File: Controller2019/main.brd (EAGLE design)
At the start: 85 x 65 mm, 95 parts, among them Q1 IPT007N06N, Q2 IPT007N06N, Q3 IPT007N06N, Q4 IPT007N06N, Q5 IPT007N06N, Q6 IPT007N06N, U1 TEENSY_3.0+4, U2 DRV8301

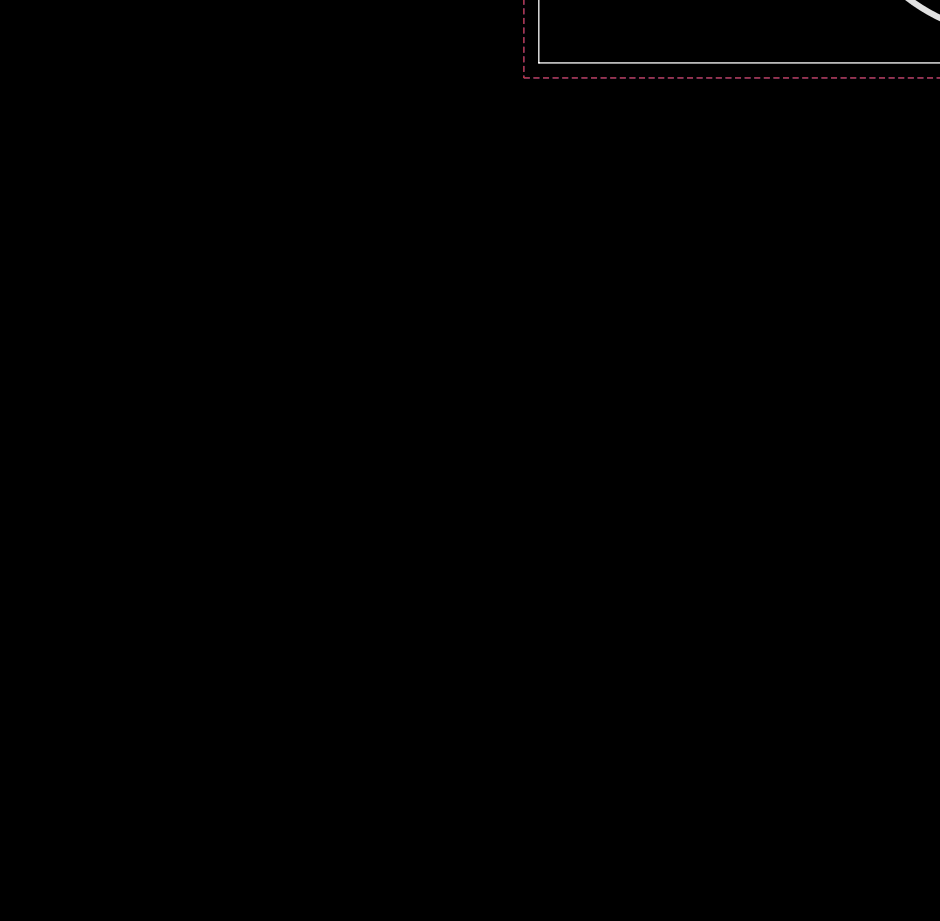
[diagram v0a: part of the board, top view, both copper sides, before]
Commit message: Added CAN Transceiver
Added CAN Transceiver to 2019 Motor Controller. Did not update board
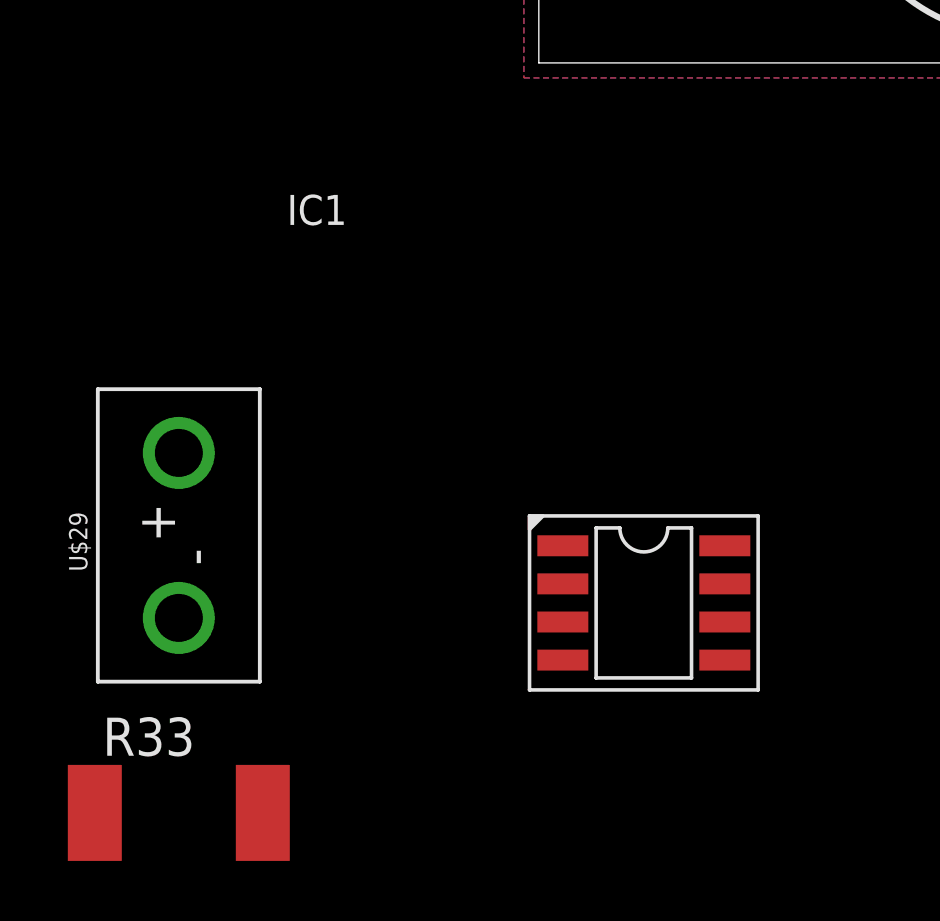
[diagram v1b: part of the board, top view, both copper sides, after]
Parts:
- added IC1: SN65HVD230D, Misaka-IC:SO-8
- added R33: 280, SparkFun-Resistors:R2512
- added U$29: HEADER2, Custom_old:2PINVALULOK
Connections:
- new net DI: IC1.1, U1.3
- new net N$18: IC1.6, R33.2, U$29.2
- new net N$19: IC1.7, R33.1, U$29.1
- new net RO: IC1.4, U1.4
- net 3.3V: now also IC1.3
- net GND: now also IC1.2
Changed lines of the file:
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@@
 <layer number="56" name="wert" color="7" fill="1" visible="no" active="no"/>
 <layer number="57" name="tCAD" color="7" fill="1" visible="no" active="no"/>
+<layer number="59" name="tCarbon" color="7" fill="1" visible="no" active="no"/>
+<layer number="60" name="bCarbon" color="7" fill="1" visible="no" active="no"/>
+<layer number="88" name="SimResults" color="9" fill="1" visible="no" active="no"/>
+<layer number="89" name="SimProbes" color="9" fill="1" visible="no" active="no"/>
 <layer number="90" name="Modules" color="5" fill="1" visible="no" active="no"/>
 <layer number="91" name="Nets" color="2" fill="1" visible="no" active="no"/>
@@
 <layer number="112" name="tSilk" color="7" fill="1" visible="no" active="yes"/>
 <layer number="113" name="IDFDebug" color="4" fill="1" visible="no" active="yes"/>
+<layer number="114" name="Badge_Outline" color="7" fill="1" visible="no" active="no"/>
+<layer number="115" name="ReferenceISLANDS" color="7" fill="1" visible="no" active="no"/>
 <layer number="116" name="Patch_BOT" color="9" fill="4" visible="no" active="yes"/>
 <layer number="118" name="Rect_Pads" color="7" fill="1" visible="no" active="no"/>
@@
 <layer number="127" name="_tValues" color="7" fill="1" visible="no" active="yes"/>
 <layer number="128" name="_bValues" color="7" fill="1" visible="no" active="yes"/>
+<layer number="129" name="Mask" color="7" fill="1" visible="no" active="no"/>
 <layer number="131" name="tAdjust" color="7" fill="1" visible="no" active="yes"/>
 <layer number="132" name="bAdjust" color="7" fill="1" visible="no" active="yes"/>
@@
 <layer number="223" name="223bmp" color="24" fill="1" visible="no" active="no"/>
 <layer number="224" name="224bmp" color="25" fill="1" visible="no" active="no"/>
+<layer number="225" name="225bmp" color="7" fill="1" visible="no" active="no"/>
+<layer number="226" name="226bmp" color="7" fill="1" visible="no" active="no"/>
+<layer number="227" name="227bmp" color="7" fill="1" visible="no" active="no"/>
+<layer number="228" name="228bmp" color="7" fill="1" visible="no" active="no"/>
+<layer number="229" name="229bmp" color="7" fill="1" visible="no" active="no"/>
+<layer number="230" name="230bmp" color="7" fill="1" visible="no" active="no"/>
 <layer number="231" name="Eagle3D_PG1" color="7" fill="1" visible="no" active="no"/>
 <layer number="232" name="Eagle3D_PG2" color="7" fill="1" visible="no" active="no"/>
@@
 </element>
 <element name="U$28" library="F-J" package="DEV" value="DEV" x="49.3533" y="53.7428" rot="MR0"/>
+<element name="IC1" library="Misaka-IC" package="SO-8" value="SN65HVD230D" x="3.5" y="-18">
+<attribute name="NAME" x="-8.4" y="-5.4" size="1" layer="25" font="vector" ratio="15"/>
+<attribute name="VALUE" x="-8.4" y="-12.6" size="1" layer="27" font="vector" ratio="15"/>
+</element>
+<element name="U$29" library="Custom_old" package="2PINVALULOK" value="HEADER2" x="-12" y="-18.5">
+<attribute name="NAME" x="-15.048" y="-15.96" size="0.6096" layer="21" rot="R90" align="bottom-center"/>
+</element>
+<element name="R33" library="SparkFun-Resistors" package="R2512" value="280" x="-12" y="-25">
+<attribute name="NAME" x="-14.54" y="-23.095" size="1.27" layer="25"/>
+<attribute name="VALUE" x="-14.54" y="-28.175" size="1.27" layer="27"/>
+</element>
 </elements>
 <signals>
@@
 <via x="58" y="9" extent="1-16" drill="0.6"/>
 <via x="58" y="7.5" extent="1-16" drill="0.6"/>
+<contactref element="IC1" pad="2"/>
+<wire x1="16" y1="4.46" x2="0.8" y2="-17.365" width="0" layer="19" extent="1-1"/>
 </signal>
 <signal name="INH_A">
@@
 <wire x1="49" y1="39.5" x2="48.65" y2="39.15" width="0.254" layer="1"/>
 <wire x1="48.65" y1="39.15" x2="48" y2="39.15" width="0.254" layer="1"/>
+<contactref element="IC1" pad="3"/>
+<wire x1="0.8" y1="-18.635" x2="50" y2="13" width="0" layer="19" extent="1-1"/>
 </signal>
 <signal name="N$13">
@@
 <wire x1="70.5" y1="23" x2="70.8678" y2="23" width="0.254" layer="1"/>
 </signal>
+<signal name="N$18">
+<contactref element="IC1" pad="6"/>
+<contactref element="R33" pad="2"/>
+<contactref element="U$29" pad="2"/>
+<wire x1="-12" y1="-18.5" x2="-9.2" y2="-25" width="0" layer="19" extent="1-1"/>
+<wire x1="6.2" y1="-18.635" x2="-9.2" y2="-25" width="0" layer="19" extent="1-1"/>
+</signal>
+<signal name="N$19">
+<contactref element="U$29" pad="1"/>
+<contactref element="R33" pad="1"/>
+<contactref element="IC1" pad="7"/>
+<wire x1="-12" y1="-13" x2="-14.8" y2="-25" width="0" layer="19" extent="1-1"/>
+<wire x1="6.2" y1="-17.365" x2="-12" y2="-13" width="0" layer="19" extent="1-1"/>
+</signal>
+<signal name="RO">
+<contactref element="IC1" pad="4"/>
+<contactref element="U1" pad="4"/>
+<wire x1="0.8" y1="-19.905" x2="66.581" y2="42.018" width="0" layer="19" extent="1-1"/>
+</signal>
+<signal name="DI">
+<contactref element="IC1" pad="1"/>
+<contactref element="U1" pad="3"/>
+<wire x1="0.8" y1="-16.095" x2="66.581" y2="39.478" width="0" layer="19" extent="1-1"/>
+</signal>
 </signals>

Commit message: route fixes, routed CAN transciever
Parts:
- removed U$29: HEADER2, Custom_old:2PINVALULOK
- added CAN: HEADER2, Custom_old:2PINVALULOK
- C12, C13, C15, C17, C18, C19, C20, C25, C29, C30, C40, C8, C9: device SparkFun-Capacitors:0603-CAP -> SparkFun-Passives:0603-CAP
- R1, R10, R11, R12, R13, R15, R16, R2, R20, R21, R22, R23, R24, R27, R28, R29, R3, R30, R31, R32, R7, R8, R9: device SparkFun-Resistors:0603-RES -> SparkFun-Passives:0603-RES
- R33: value 280 -> 120; device SparkFun-Resistors:R2512 -> SparkFun-Passives:0603-RES
- moved R33 95.2 mm to (71.3, 21.1), flipped to the bottom, turned to 90 degrees
- moved IC1 74.1 mm to (66.5, 21.0), flipped to the bottom, turned to 180 degrees
- moved R24 25.2 mm to (63.5, 37.4), turned to 0 degrees
- moved R5 22.8 mm to (63.5, 35.4), turned to 0 degrees
- moved U$2 6.00 mm to (75.0, 23.0)
- moved U$15 2.00 mm to (75.0, 43.0)
- moved R25 1.87 mm to (63.5, 33.7), turned to 0 degrees
- moved R23 1.77 mm to (63.5, 40.7), turned to 0 degrees
- moved R22 1.58 mm to (63.5, 39.0), turned to 0 degrees
- moved R6 1.58 mm to (63.5, 32.0), turned to 0 degrees
- moved U$17 1.00 mm to (75.0, 55.0)
- moved C8 0.40 mm to (66.2, 14.7)
- moved R17 0.10 mm to (54.9, 50.0)
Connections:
- net N$13 renamed ENC_C_RAW
- net N$14 renamed ENC_A_RAW
- net N$15 renamed ENC_B_RAW
- removed net N$18: IC1.6, R33.2, U$29.2
- removed net N$19: IC1.7, R33.1, U$29.1
- new net CANH: CAN.1, IC1.7, R33.1
- new net CANL: CAN.2, IC1.6, R33.2
- new net EN_CAN: IC1.8, U1.A11
- net CS_ENC: now also U1.A10
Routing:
- net EN_CAN: track 0.00 -> 33.1 mm, vias 0 -> 2
- net ENC_C: track 34.6 -> 2.87 mm, vias 7 -> 0
- net DI: track 0.00 -> 26.1 mm, vias 0 -> 1
- net CS_ENC: track 17.7 -> 43.2 mm, vias 2 -> 4
- net RO: track 0.00 -> 22.7 mm, vias 0 -> 1
- net ENC_C_RAW: track 16.6 -> 36.4 mm, vias 0 -> 3
- net CANH: track 0.00 -> 17.5 mm
- net CANL: track 0.00 -> 12.8 mm
- net INH_A: track 61.2 -> 49.1 mm, vias 3 -> 1
- net ENC_B_RAW: track 25.5 -> 35.7 mm
- net MISO: track 85.4 -> 95.3 mm
- net ENC_B: track 7.68 -> 2.52 mm, vias 2 -> 0
- net MOSI: track 86.8 -> 91.8 mm
- net 3.3V: track 80.1 -> 85.0 mm, vias 4 -> 5
- net INL_C: track 35.6 -> 31.4 mm
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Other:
- board text added: "CAN"
- board text added: "Designed by GDC, JP, PLG, AM for the Shell Eco Marathon"
- board text added: "H"
- board text added: "L"
- board text added: "Motor Controller Rev 2.1 Nov 2018"
- board text removed: "Designed by PLG and AM for the Shell Eco Marathon"
- board text removed: "Motor Controller Rev 2 Feb 2017"
